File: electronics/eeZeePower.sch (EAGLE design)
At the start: 10 parts

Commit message: Updated version #
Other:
- note added: "0.6"
- note removed: "0.4"
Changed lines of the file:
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@@
 <plain>
 <text x="160.528" y="23.622" size="3.81" layer="94">eeZee Power</text>
-<text x="233.934" y="24.13" size="3.81" layer="94">0.4</text>
+<text x="233.934" y="24.13" size="3.81" layer="94">0.6</text>
 <text x="129.54" y="99.06" size="1.778" layer="91">HEATSINK</text>
 </plain>

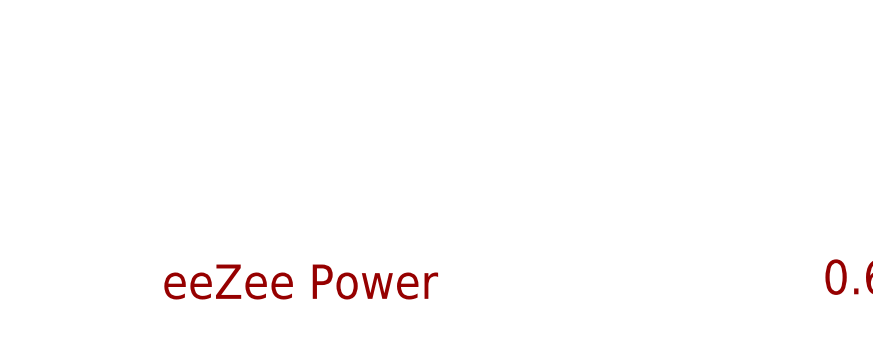
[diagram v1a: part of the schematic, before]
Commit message: updated silk, updated board name to microB
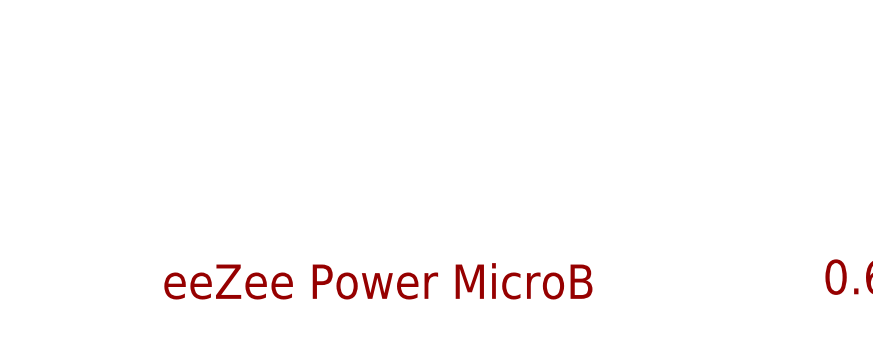
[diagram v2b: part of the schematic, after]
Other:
- note added: "eeZee Power MicroB"
- note removed: "eeZee Power"
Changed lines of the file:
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@@
 <sheet>
 <plain>
-<text x="160.528" y="23.622" size="3.81" layer="94">eeZee Power</text>
+<text x="160.528" y="23.622" size="3.81" layer="94">eeZee Power MicroB</text>
 <text x="233.934" y="24.13" size="3.81" layer="94">0.6</text>
 <text x="129.54" y="99.06" size="1.778" layer="91">HEATSINK</text>
